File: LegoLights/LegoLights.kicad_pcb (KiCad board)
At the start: 2 copper layers, 30.5 x 7.6 mm, 4 parts, among them J1 Conn_01x02, J2 Conn_01x02

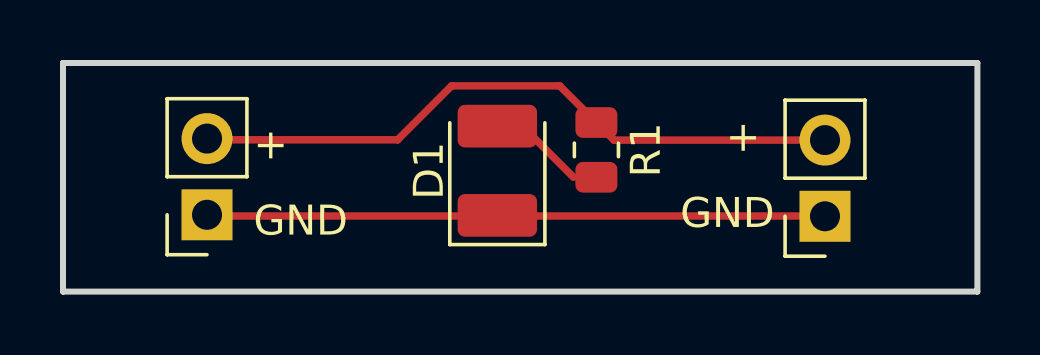
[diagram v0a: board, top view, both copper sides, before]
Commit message: Use filled zones instead of lines
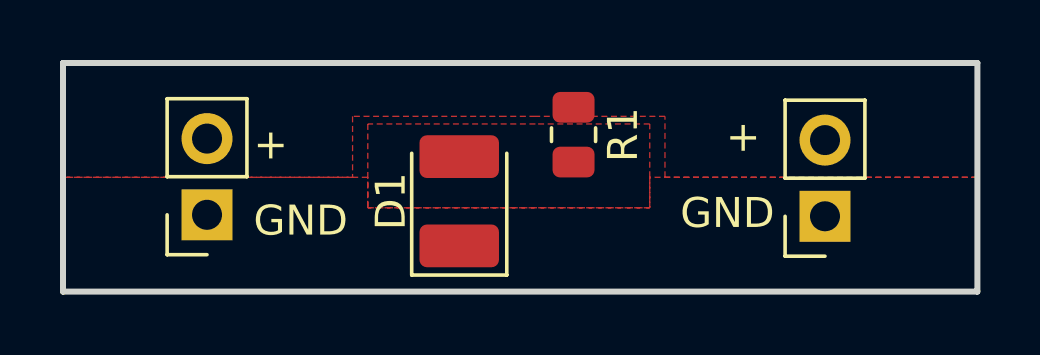
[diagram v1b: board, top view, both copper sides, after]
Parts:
- moved D1 1.63 mm to (132.6, 60.5)
- moved R1 0.92 mm to (136.4, 58.3)
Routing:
- net +12V: track 22.1 -> 0.04 mm
- net GND: track 20.6 -> 0.01 mm
- net Net-(D1-A): track 4.11 -> 0.00 mm
- added copper zone on F.Cu, net +12V
- added copper zone on F.Cu, net GND
- added copper zone on F.Cu, net Net-(D1-A)
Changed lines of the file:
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@@
   )
   (footprint "LED_SMD:LED_1210_3225Metric_Pad1.42x2.65mm_HandSolder" (layer "F.Cu")
-    (at 133.858 59.4725 90)
+    (at 132.588 60.4885 90)
     (descr "LED SMD 1210 (3225 Metric), square (rectangular) end terminal, IPC_7351 nominal, (Body size source: http://www.tortai-tech.com/upload/download/2011102023233369053.pdf), generated with kicad-footprint-generator")
     (tags "LED handsolder")
@@
   )
   (footprint "Resistor_SMD:R_0805_2012Metric" (layer "F.Cu")
-    (at 137.16 58.7775 -90)
+    (at 136.398 58.2695 -90)
     (descr "Resistor SMD 0805 (2012 Metric), square (rectangular) end terminal, IPC_7351 nominal, (Body size source: IPC-SM-782 page 72, https://www.pcb-3d.com/wordpress/wp-content/uploads/ipc-sm-782a_amendment_1_and_2.pdf), generated with kicad-footprint-generator")
     (tags "resistor")
@@
     (effects (font (size 1 1) (thickness 0.15)) (justify left bottom))
   )
-  (segment (start 134.693 57.985) (end 133.858 57.985) (width 0.25) (layer "F.Cu") (net 1))
-  (segment (start 136.398 59.69) (end 134.693 57.985) (width 0.25) (layer "F.Cu") (net 1))
-  (segment (start 133.858 58.42) (end 134.7235 58.42) (width 0.25) (layer "F.Cu") (net 1))
   (segment (start 144.78 60.99) (end 144.77 60.98) (width 0.25) (layer "F.Cu") (net 2))
-  (segment (start 144.77 60.98) (end 124.186 60.98) (width 0.25) (layer "F.Cu") (net 2))
-  (segment (start 137.16 57.865) (end 135.937 56.642) (width 0.25) (layer "F.Cu") (net 3))
-  (segment (start 137.745 58.45) (end 137.16 57.865) (width 0.25) (layer "F.Cu") (net 3))
-  (segment (start 132.334 56.642) (end 130.536 58.44) (width 0.25) (layer "F.Cu") (net 3))
-  (segment (start 144.78 58.45) (end 137.745 58.45) (width 0.25) (layer "F.Cu") (net 3))
-  (segment (start 130.536 58.44) (end 124.186 58.44) (width 0.25) (layer "F.Cu") (net 3))
   (segment (start 144.78 58.45) (end 144.75 58.42) (width 0.25) (layer "F.Cu") (net 3))
-  (segment (start 135.937 56.642) (end 132.334 56.642) (width 0.25) (layer "F.Cu") (net 3))
+  (zone (net 1) (net_name "Net-(D1-A)") (layer "F.Cu") (hatch edge 0.5)
+    (priority 1)
+    (connect_pads (clearance 0.5))
+    (min_thickness 0.25) (filled_areas_thickness no)
+    (fill yes (thermal_gap 0.5) (thermal_bridge_width 0.5))
+    (polygon
+      (pts
+        (xy 138.938 59.69)
+        (xy 138.938 57.912)
+        (xy 135.128 57.912)
+        (xy 133.858 57.912)
+        (xy 131.318 57.912)
+        (xy 129.54 57.912)
+        (xy 129.54 60.706)
+        (xy 138.938 60.706)
+      )
+    )
+  )
+  (zone (net 3) (net_name "+12V") (layer "F.Cu") (hatch edge 0.5)
+    (priority 2)
+    (connect_pads (clearance 0.5))
+    (min_thickness 0.25) (filled_areas_thickness no)
+    (fill yes (thermal_gap 0.5) (thermal_bridge_width 0.5))
+    (polygon
+      (pts
+        (xy 149.86 59.69)
+        (xy 139.446 59.69)
+        (xy 139.446 57.658)
+        (xy 135.128 57.658)
+        (xy 134.112 57.658)
+        (xy 130.556 57.658)
+        (xy 129.032 57.658)
+        (xy 129.032 59.69)
+        (xy 125.476 59.69)
+        (xy 119.38 59.69)
+        (xy 119.38 55.88)
+        (xy 149.86 55.88)
+      )
+    )
+  )
+  (zone (net 2) (net_name "GND") (layer "F.Cu") (hatch edge 0.5)
+    (connect_pads (clearance 0.5))
+    (min_thickness 0.25) (filled_areas_thickness no)
+    (fill yes (thermal_gap 0.5) (thermal_bridge_width 0.5))
+    (polygon
+      (pts
+        (xy 149.86 59.69)
+        (xy 138.938 59.69)
+        (xy 138.938 60.706)
+        (xy 129.54 60.706)
+        (xy 129.54 59.69)
+        (xy 119.38 59.69)
+        (xy 119.38 63.5)
+        (xy 149.86 63.5)
+      )
+    )
+  )
 )
